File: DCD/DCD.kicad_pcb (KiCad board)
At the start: 4 copper layers, 110 x 110 mm, 164 parts, among them IC1 830S21AMI-01LF, IC2 830S21AMI-01LF, J1 UMPS-04-03.5-G-VT-SM-WT, J2 UMPS-04-03.5-G-VT-SM-WT, J3 UMPS-04-03.5-G-VT-SM-WT, J4 UMPS-04-03.5-G-VT-SM-WT, J5 Conn_01x02_Pin, U1 TLV76780DBVR, U10 OPA277UA, U11 DAC8811ICDGKT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

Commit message: Layout mostly done
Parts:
- removed the C23 at (185.6, 110.2)
- removed J5: Conn_01x02_Pin, Connector_PinHeader_2.54mm:PinHeader_1x02_P2.54mm_Vertical
- moved FB15 26.8 mm to (140.8, 131.5)
- moved FB27 17.7 mm to (186.0, 100.8), turned to 90 degrees
- moved R2 15.7 mm to (155.8, 140.6), turned to 180 degrees
- moved C63 14.4 mm to (189.0, 100.8), turned to -90 degrees
- moved C25 12.8 mm to (166.0, 141.1), turned to -90 degrees
- moved Y1 11.9 mm to (157.8, 137.1), turned to 0 degrees
- moved U8 11.9 mm to (164.8, 137.8), turned to 0 degrees
- moved C62 11.5 mm to (187.5, 100.8), turned to -90 degrees
- moved FB21 10.6 mm to (153.2, 135.9), turned to 0 degrees
- moved C61 10.6 mm to (187.2, 104.0)
- moved C57 10.2 mm to (150.0, 137.4), turned to -90 degrees
- moved C56 10.0 mm to (135.0, 124.2)
- moved FB26 9.61 mm to (187.2, 108.0), turned to 90 degrees
- moved C60 9.45 mm to (190.2, 108.0), turned to -90 degrees
- moved C58 9.19 mm to (159.8, 141.4), turned to 180 degrees
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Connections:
- U8 pad 3: CS_CLK -> CNV_CLK
- U8 pad 5: /Comms/Signal Reconditioning/CLK -> /Comms/CLK
- U8 pad 7: /Comms/CLK -> CS_CLK
- U8 pad 8: CNV_CLK -> /Comms/Signal Reconditioning/CLK
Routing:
- net 3V3_CLK: track 0.00 -> 190.9 mm, vias 0 -> 2
- net Net-(U3-VOUT): track 16.1 -> 110.1 mm
- net Net-(U1-OUT): track 106.3 -> 186.4 mm
- net /Comms/Signal Reconditioning/CNV: track 0.00 -> 37.5 mm, vias 0 -> 1
- net Net-(J3-Pin_3): track 4.77 -> 37.9 mm
- net /ADC/5V: track 6.12 -> 32.9 mm
- net /Comms/-Vin: track 126.9 -> 141.8 mm
- net /Comms/7V: track 0.00 -> 10.3 mm
- net Net-(Y1-VDD): track 0.00 -> 10.2 mm
- net Net-(U8-VDD): track 0.00 -> 8.23 mm
- net Net-(J2-Pin_1): track 0.00 -> 5.34 mm, vias 0 -> 1
- net /ADC/7V: track 73.1 -> 68.3 mm
- net Net-(U15-VCC): track 0.00 -> 4.79 mm
- net Net-(IC2-VDD): track 0.00 -> 4.75 mm
- net Net-(U16-VCC): track 0.00 -> 4.68 mm
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
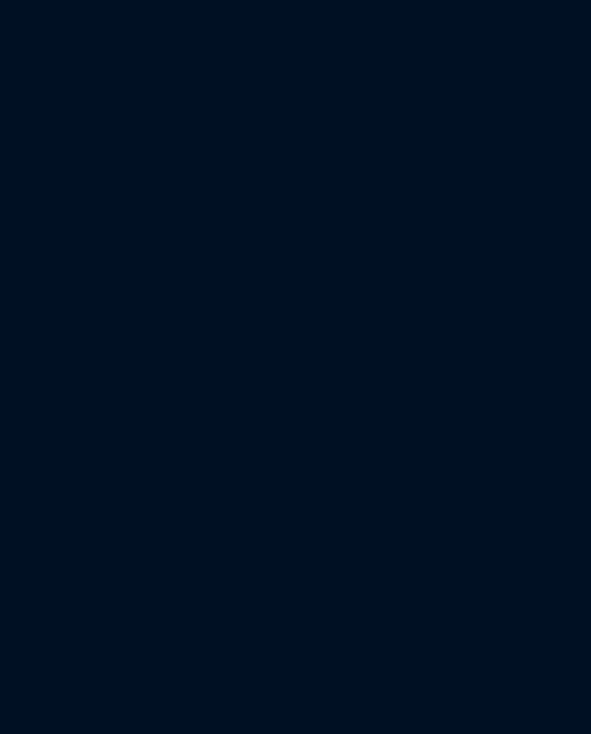
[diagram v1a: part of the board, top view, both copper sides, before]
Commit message: Added the footprint
My libraries are fucked for some reason so I have to change machines to
pull footprints and add components
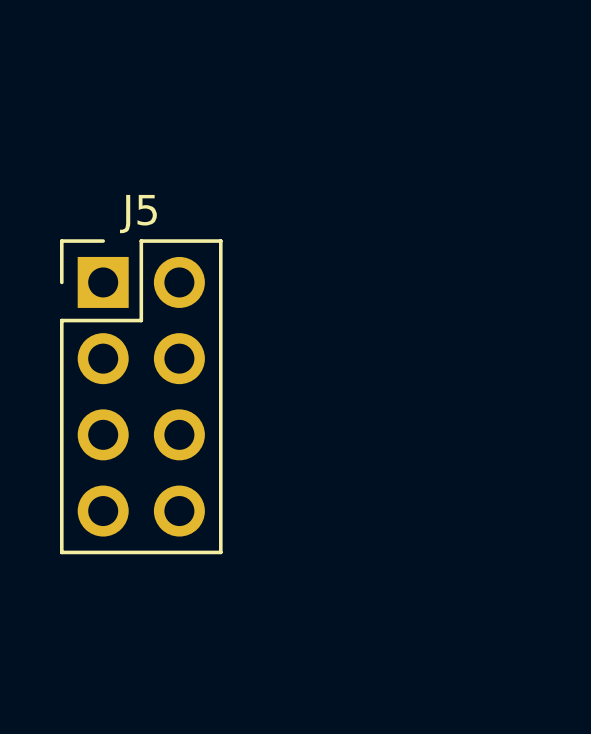
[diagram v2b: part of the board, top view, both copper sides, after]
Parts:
- added J5: Conn_02x04_Top_Bottom, Connector_PinHeader_2.54mm:PinHeader_2x04_P2.54mm_Vertical, F.Cu at (74.7, 104.1)
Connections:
- IC1 pad 7: /Comms/*CS -> /Comms/*CS2
- U11 pad 1: /Comms/CLK -> /Comms/CLK1
- U11 pad 8: /Comms/*CS -> /Comms/*CS1
- U12 pad 1: /Comms/CLK -> /Comms/CLK2
- U12 pad 8: /Comms/*CS -> /Comms/*CS2
- U8 pad 5: /Comms/CLK -> /Comms/CLK2

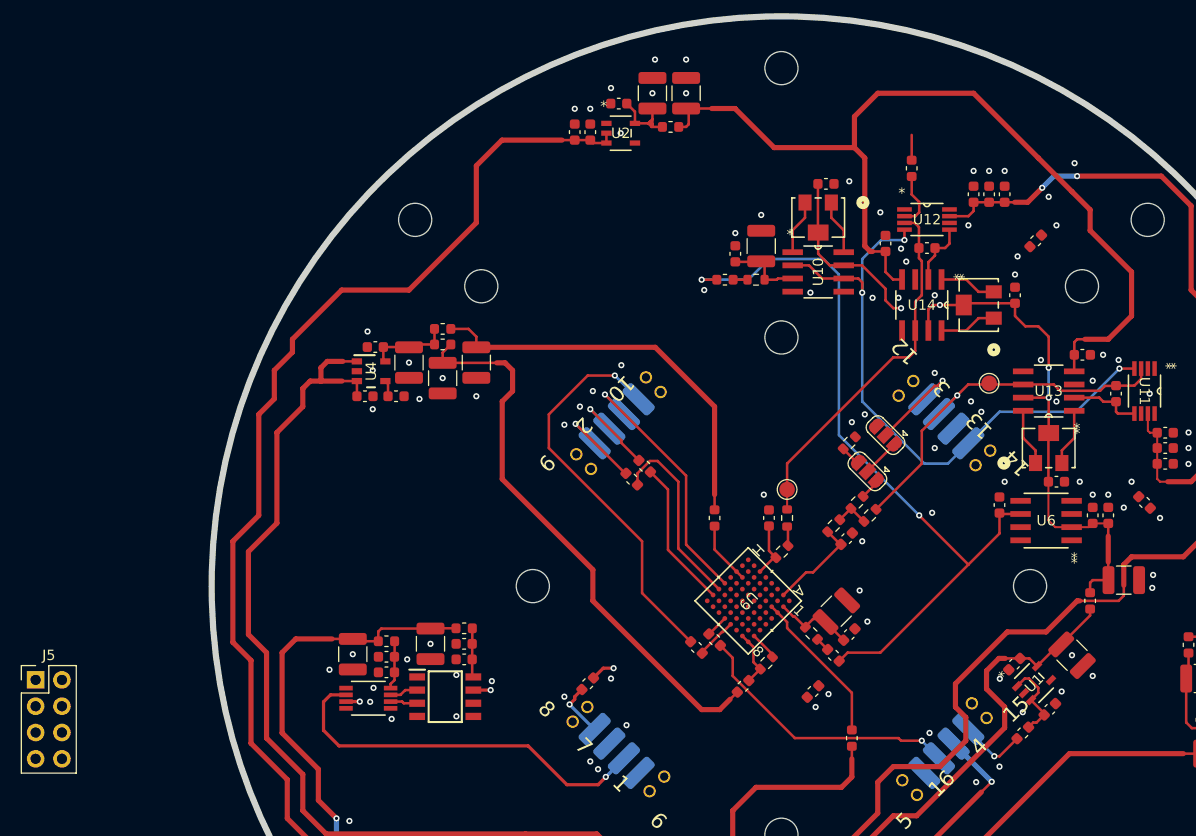
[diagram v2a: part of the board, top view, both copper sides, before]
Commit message: Almost finished the layout. Did all of the power and top layer
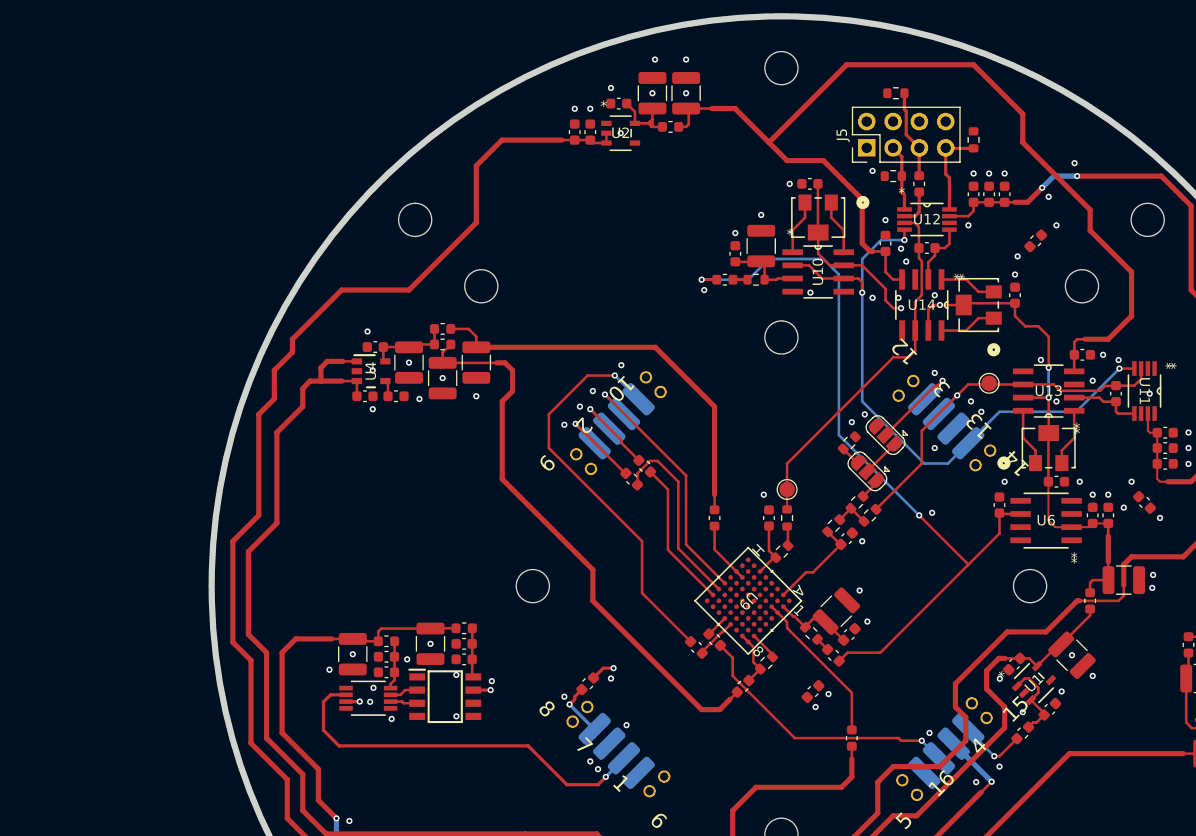
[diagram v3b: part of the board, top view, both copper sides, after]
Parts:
- added R3: 10k, Resistor_SMD:R_0603_1608Metric, F.Cu at (157.5, 55.5)
- added R4: 10k, Resistor_SMD:R_0603_1608Metric, F.Cu at (165.2, 52.0)
- added R5: 10k, Resistor_SMD:R_0603_1608Metric, F.Cu at (157.8, 47.5)
- moved J5 95.3 mm to (154.9, 52.8), turned to 90 degrees
- moved FB11 1.67 mm to (160.0, 56.2)
- moved C46 1.55 mm to (149.4, 56.2), turned to 180 degrees
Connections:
- IC1 pad 7: /Comms/*CS2 -> /Comms/*CS1
- J5 pad 3: /ADC/DGND -> /Comms/CLK2
- J5 pad 7: /Comms/*CS1 -> /Comms/*CS2
- J5 pad 8: /Comms/CLK1 -> /ADC/DGND
- U8 pad 5: /Comms/CLK2 -> /Comms/CLK1
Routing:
- net /Comms/*CS2: track 0.00 -> 8.80 mm
- net /DAC/-1.2V: track 89.2 -> 96.9 mm
- net /Comms/CLK2: track 0.00 -> 6.40 mm
- net Net-(J5-Pin_5): track 2.44 -> 8.57 mm
- net /Comms/SDI2: track 5.34 -> 3.52 mm
- net /ADC/DGND: vias 84 -> 85

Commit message: Progrezz
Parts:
- moved C35 10.3 mm to (174.8, 134.0), turned to -45 degrees
- moved FB25 10.2 mm to (172.7, 137.1), turned to 45 degrees
- moved C58 9.95 mm to (169.5, 139.6), turned to -135 degrees
- moved C25 9.90 mm to (173.8, 135.0), turned to -45 degrees
- moved R1 9.01 mm to (171.7, 136.1), turned to -135 degrees
- moved U8 7.15 mm to (170.5, 133.5), turned to 45 degrees
- moved R2 3.53 mm to (158.8, 142.5)
- moved Y1 3.02 mm to (160.8, 136.8)
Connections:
- U8 pad 5: /Comms/CLK1 -> CS_CLK
- U8 pad 7: CS_CLK -> /Comms/CLK1
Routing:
- net /Comms/SDI1: track 2.33 -> 116.6 mm, vias 1 -> 2
- net /Comms/CLK1: track 0.00 -> 79.5 mm, vias 0 -> 2
- net CNV_CLK: track 1.33 -> 78.9 mm, vias 1 -> 2
- net /Comms/Signal Reconditioning/*CS: track 0.00 -> 73.5 mm, vias 0 -> 1
- net CS_CLK: track 0.00 -> 55.6 mm
- net /ADC/CNV: track 1.67 -> 33.8 mm, vias 1 -> 2
- net /Comms/*CS1: track 0.00 -> 28.0 mm, vias 0 -> 2
- net /Comms/Signal Reconditioning/CLK: track 0.13 -> 24.8 mm, vias 0 -> 1
- net 3V3_CLK: track 190.9 -> 205.1 mm
- net Net-(Y1-VDD): track 10.2 -> 17.2 mm
- net /ADC/VIO: track 54.4 -> 50.0 mm
- net /ADC/7V: track 68.3 -> 72.1 mm
- net Net-(U8-CLKIN): track 3.22 -> 6.80 mm
- net Net-(Y1-OE/~{ST}): track 2.58 -> 4.83 mm
- net Net-(U6-VOUT): track 74.0 -> 76.2 mm
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- added copper zone on B.Cu, net /ADC/DGND
- added copper zone on F.Cu, net /ADC/DGND
- added copper zone on In1.Cu, net /ADC/DGND
- added copper zone on In2.Cu, net /ADC/DGND

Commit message: TMP
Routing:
- net CS_CLK: track 55.6 -> 80.9 mm
- net /Comms/*CS1: track 28.0 -> 33.1 mm

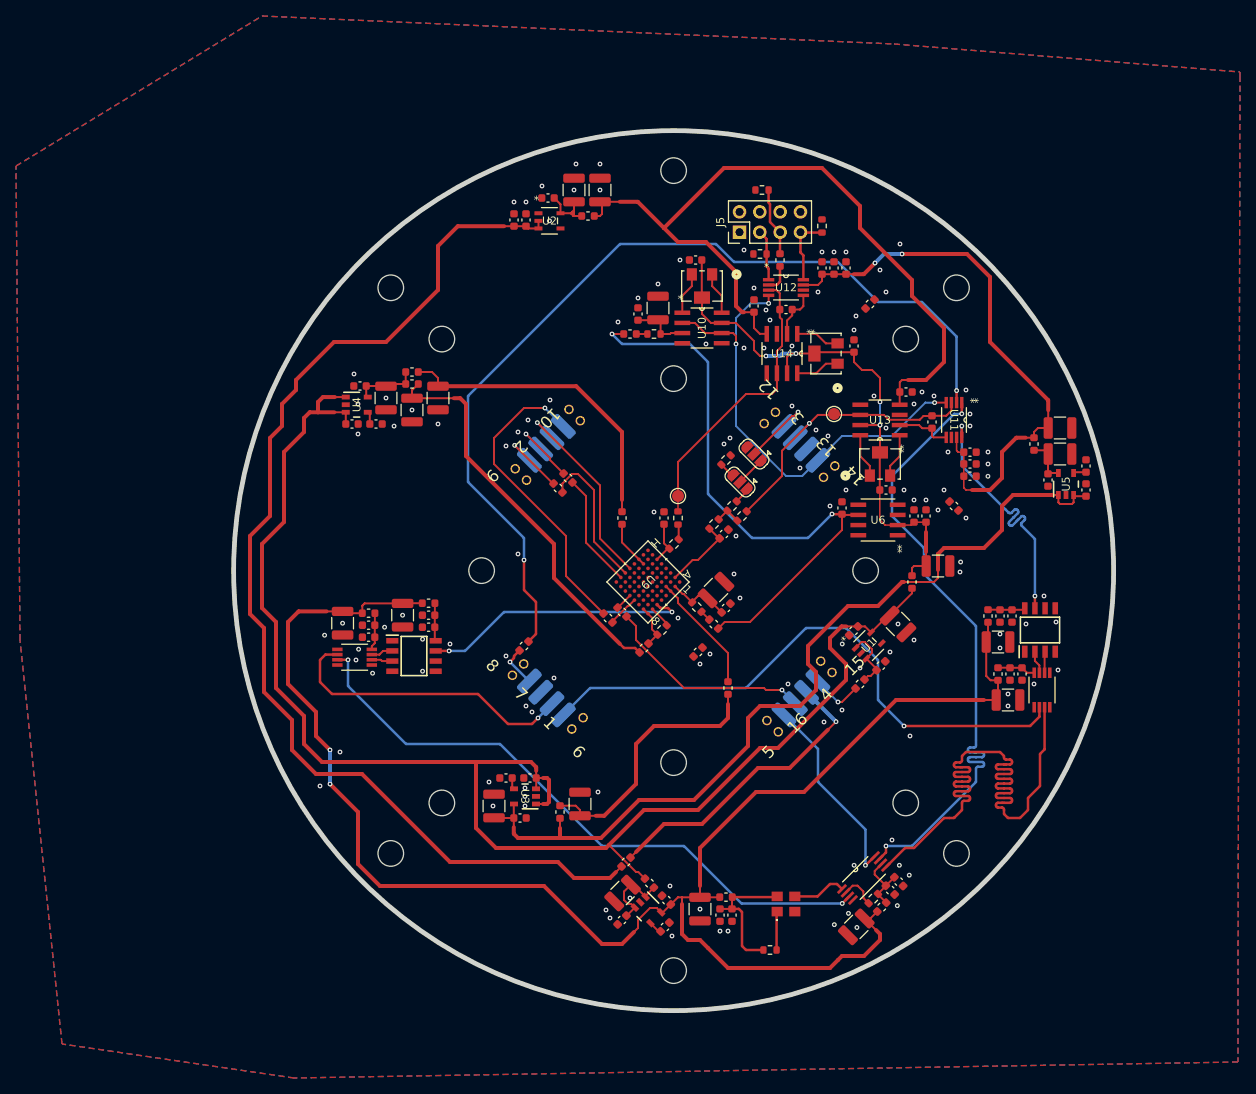
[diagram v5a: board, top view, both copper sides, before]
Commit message: Stiching ground
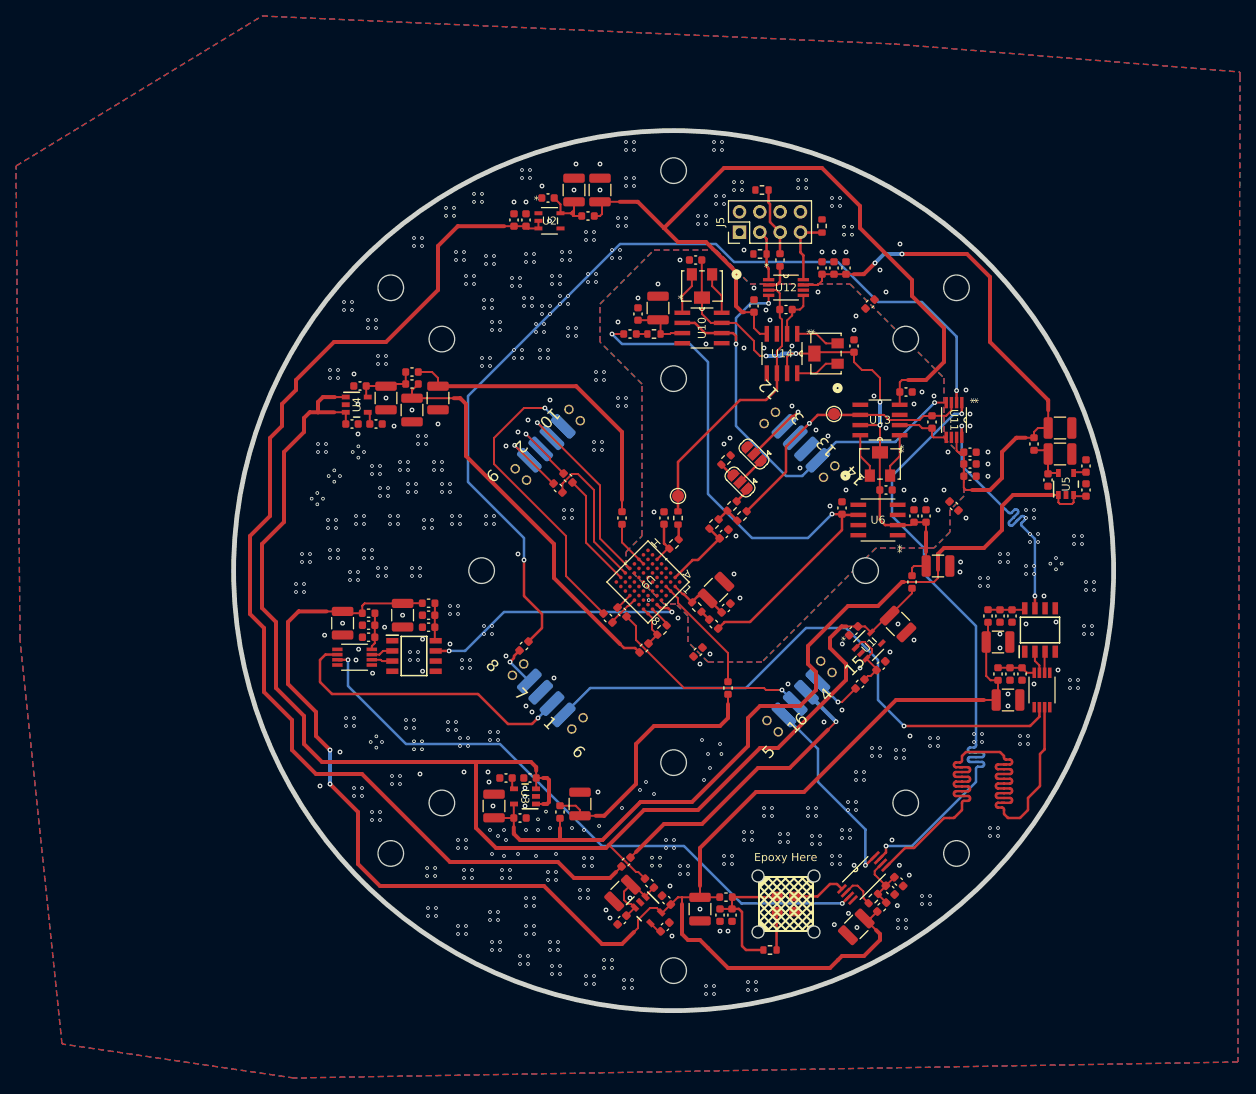
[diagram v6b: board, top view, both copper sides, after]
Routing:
- net Net-(U3-VOUT): track 110.4 -> 111.1 mm
- net /Comms/SDI1: track 116.6 -> 117.2 mm
- net /ADC/DGND: vias 95 -> 654
- added copper zone on B.Cu, net /ADC/AGND
- added copper zone on F.Cu, net /ADC/AGND
- added copper zone on In1.Cu, net /ADC/AGND
- added copper zone on In2.Cu, net /ADC/AGND
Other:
- outline, holes or cut-outs redrawn
- board text added: "Epoxy Here"

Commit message: Finished the layout
Modified ground planes separation, finished stiching, fixed drc errors
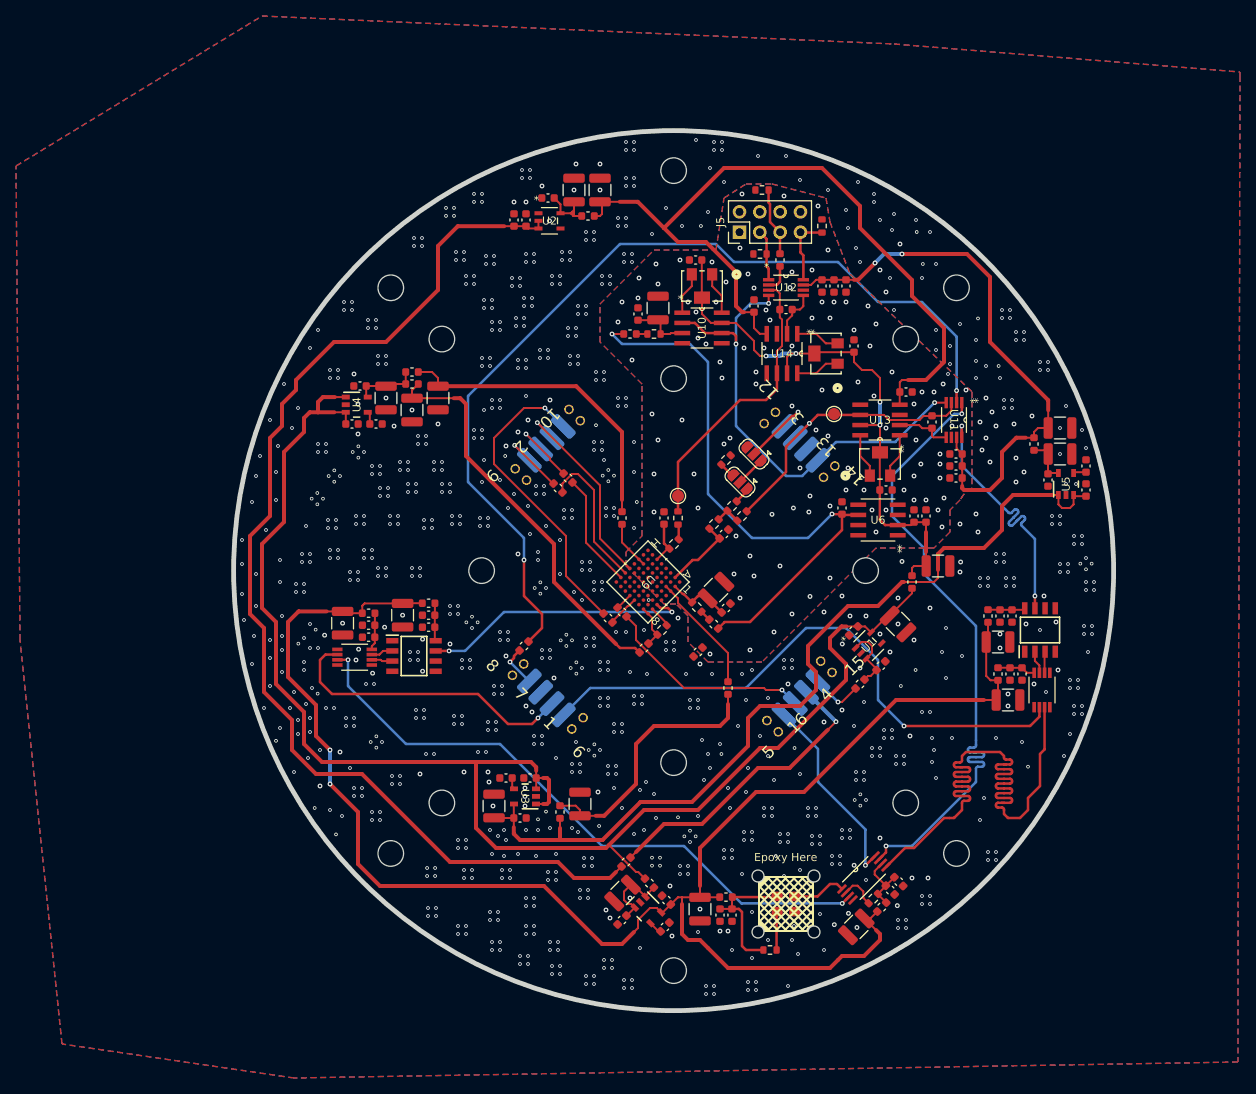
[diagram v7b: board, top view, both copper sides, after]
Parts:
- removed FB18, FB19: 470Ω, Inductor_SMD:L_0603_1608Metric
- moved C39 3.75 mm to (168.2, 59.5), turned to -90 degrees
- moved C40 3.28 mm to (182.0, 80.5), turned to 180 degrees
- moved C41 2.70 mm to (165.2, 59.5), turned to -90 degrees
- moved C42 2.70 mm to (166.8, 59.5), turned to -90 degrees
- moved C38 2.47 mm to (182.0, 83.5), turned to 180 degrees
- moved C43 2.46 mm to (182.0, 82.0), turned to 180 degrees
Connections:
- C38 pad 2: /ADC/DGND -> /ADC/AGND
- C39 pad 2: /ADC/DGND -> /ADC/AGND
- C40 pad 2: /ADC/DGND -> /ADC/AGND
- C41 pad 2: /ADC/DGND -> /ADC/AGND
- C42 pad 2: /ADC/DGND -> /ADC/AGND
- C43 pad 2: /ADC/DGND -> /ADC/AGND
- J5 pad 1: /ADC/DGND -> /ADC/AGND
- J5 pad 2: /ADC/DGND -> /ADC/AGND
- J5 pad 4: /ADC/DGND -> /ADC/AGND
- J5 pad 6: /ADC/DGND -> /ADC/AGND
- J5 pad 8: /ADC/DGND -> /ADC/AGND
- R3 pad 2: /ADC/DGND -> /ADC/AGND
- R4 pad 2: /ADC/DGND -> /ADC/AGND
- R5 pad 2: /ADC/DGND -> /ADC/AGND
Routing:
- net Net-(U3-VOUT): track 111.1 -> 111.8 mm
- net /ADC/DGND: vias 654 -> 957
- net /ADC/AGND: vias 37 -> 101

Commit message: Added biasing and termination resistors for the logic gates
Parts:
- added R12: 127, Resistor_SMD:R_0603_1608Metric, F.Cu at (81.2, 111.5)
- added R13: 82, Resistor_SMD:R_0603_1608Metric, F.Cu at (81.2, 114.0)
- added R21: 127, Resistor_SMD:R_0603_1608Metric, F.Cu at (81.2, 116.5)
- added R22: 82, Resistor_SMD:R_0603_1608Metric, F.Cu at (81.2, 119.0)
- added R6: 127, Resistor_SMD:R_0603_1608Metric, F.Cu at (81.2, 101.4)
- added R7: 82, Resistor_SMD:R_0603_1608Metric, F.Cu at (81.2, 103.9)
- added R8: 127, Resistor_SMD:R_0603_1608Metric, F.Cu at (81.2, 106.5)
- added R9: 82, Resistor_SMD:R_0603_1608Metric, F.Cu at (81.2, 109.0)
- moved FB20 3.02 mm to (148.5, 102.5), turned to 180 degrees
- moved IC1 2.97 mm to (192.8, 99.5)
- moved C61 1.46 mm to (186.5, 102.8)
- moved C62 1.46 mm to (186.8, 99.5)
- moved C63 1.46 mm to (188.2, 99.5)
- moved FB27 1.46 mm to (185.2, 99.5)
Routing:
- net /Comms/*CS1: track 33.1 -> 19.3 mm
- net 3V3_CLK: track 205.1 -> 200.8 mm
- net Net-(IC1-CLK): track 2.87 -> 0.00 mm
- net Net-(IC1-NCLK): track 2.66 -> 0.08 mm
- net Net-(IC1-VDD): track 4.68 -> 3.27 mm
- net /ADC/DGND: vias 957 -> 945
- net /ADC/AGND: vias 101 -> 107
